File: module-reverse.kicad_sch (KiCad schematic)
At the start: 13 parts, among them J1 Screw_Terminal_01x02, J10 Screw_Terminal_01x05, J11 Screw_Terminal_01x05, J2 Screw_Terminal_01x02, J7 Screw_Terminal_01x02, J8 Screw_Terminal_01x02, J9 Screw_Terminal_01x02, K1 AZ733-2CE-12DE, U1 L7812

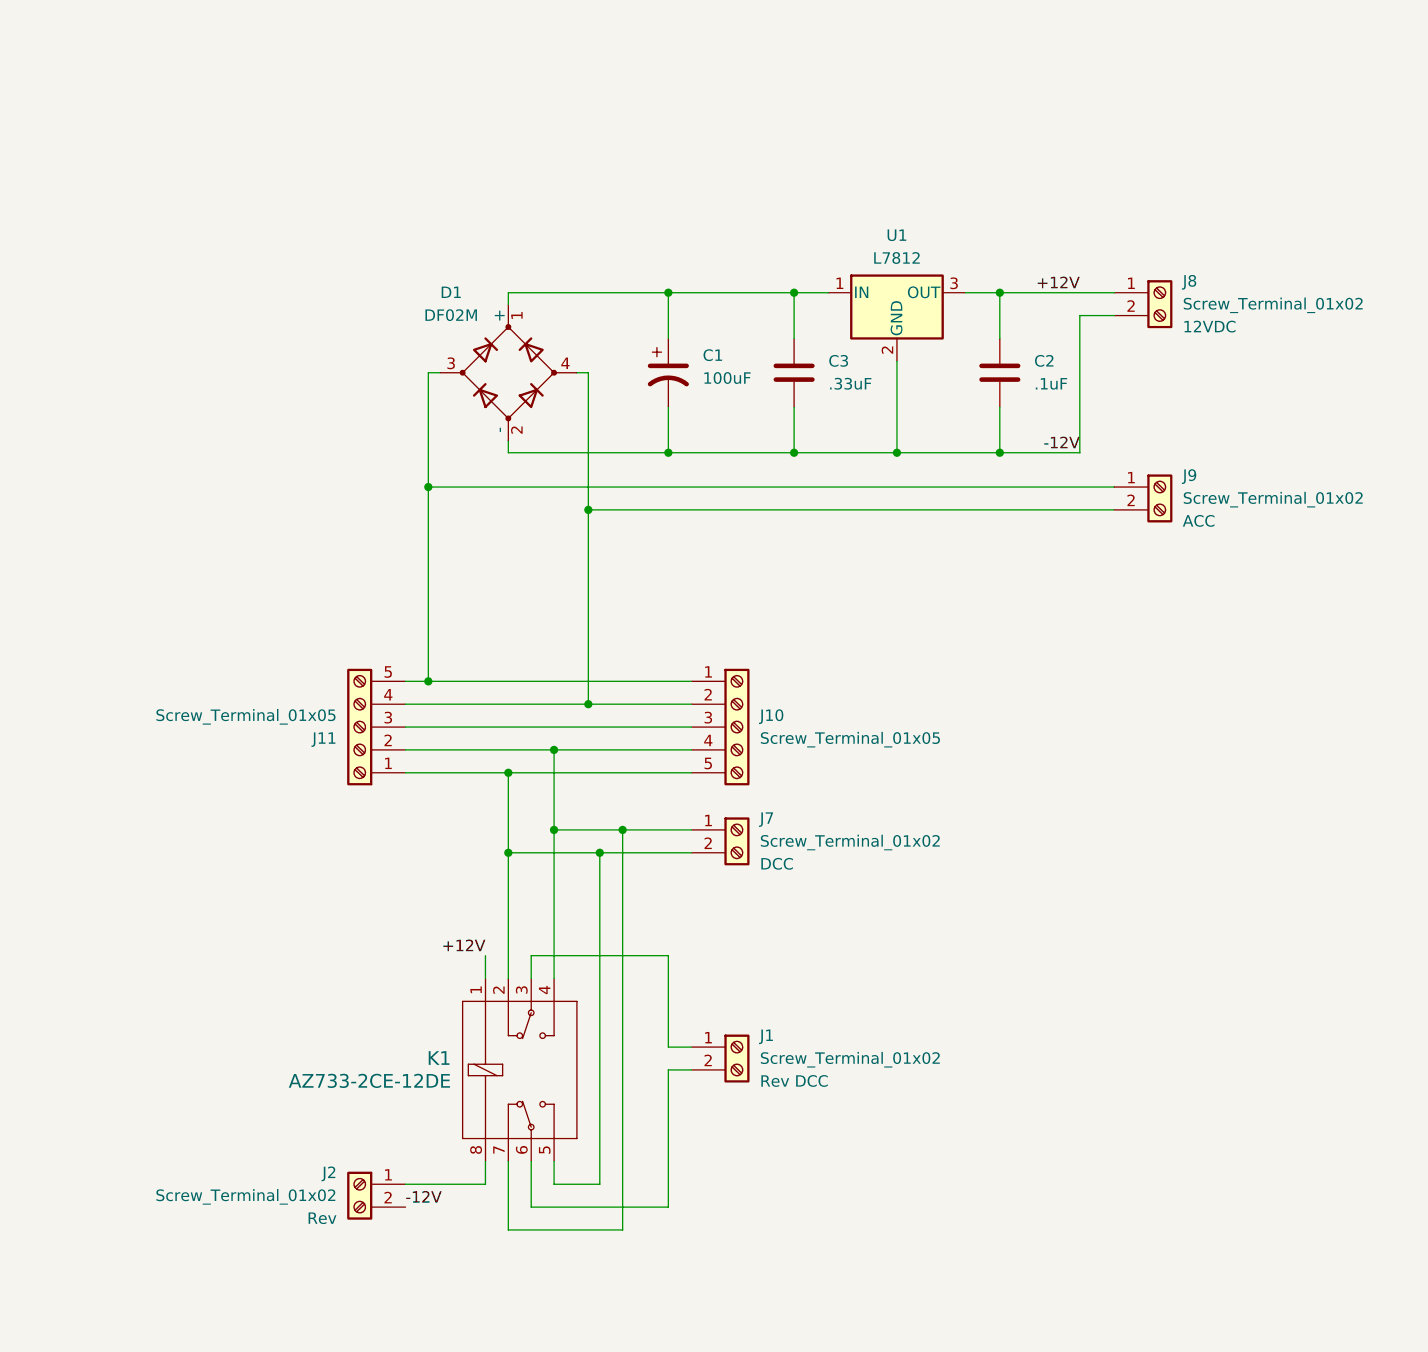
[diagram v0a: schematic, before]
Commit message: Changed the reversing output to have both Normal and Reverse outputs that go to the two branches instead of a single output that reverses.
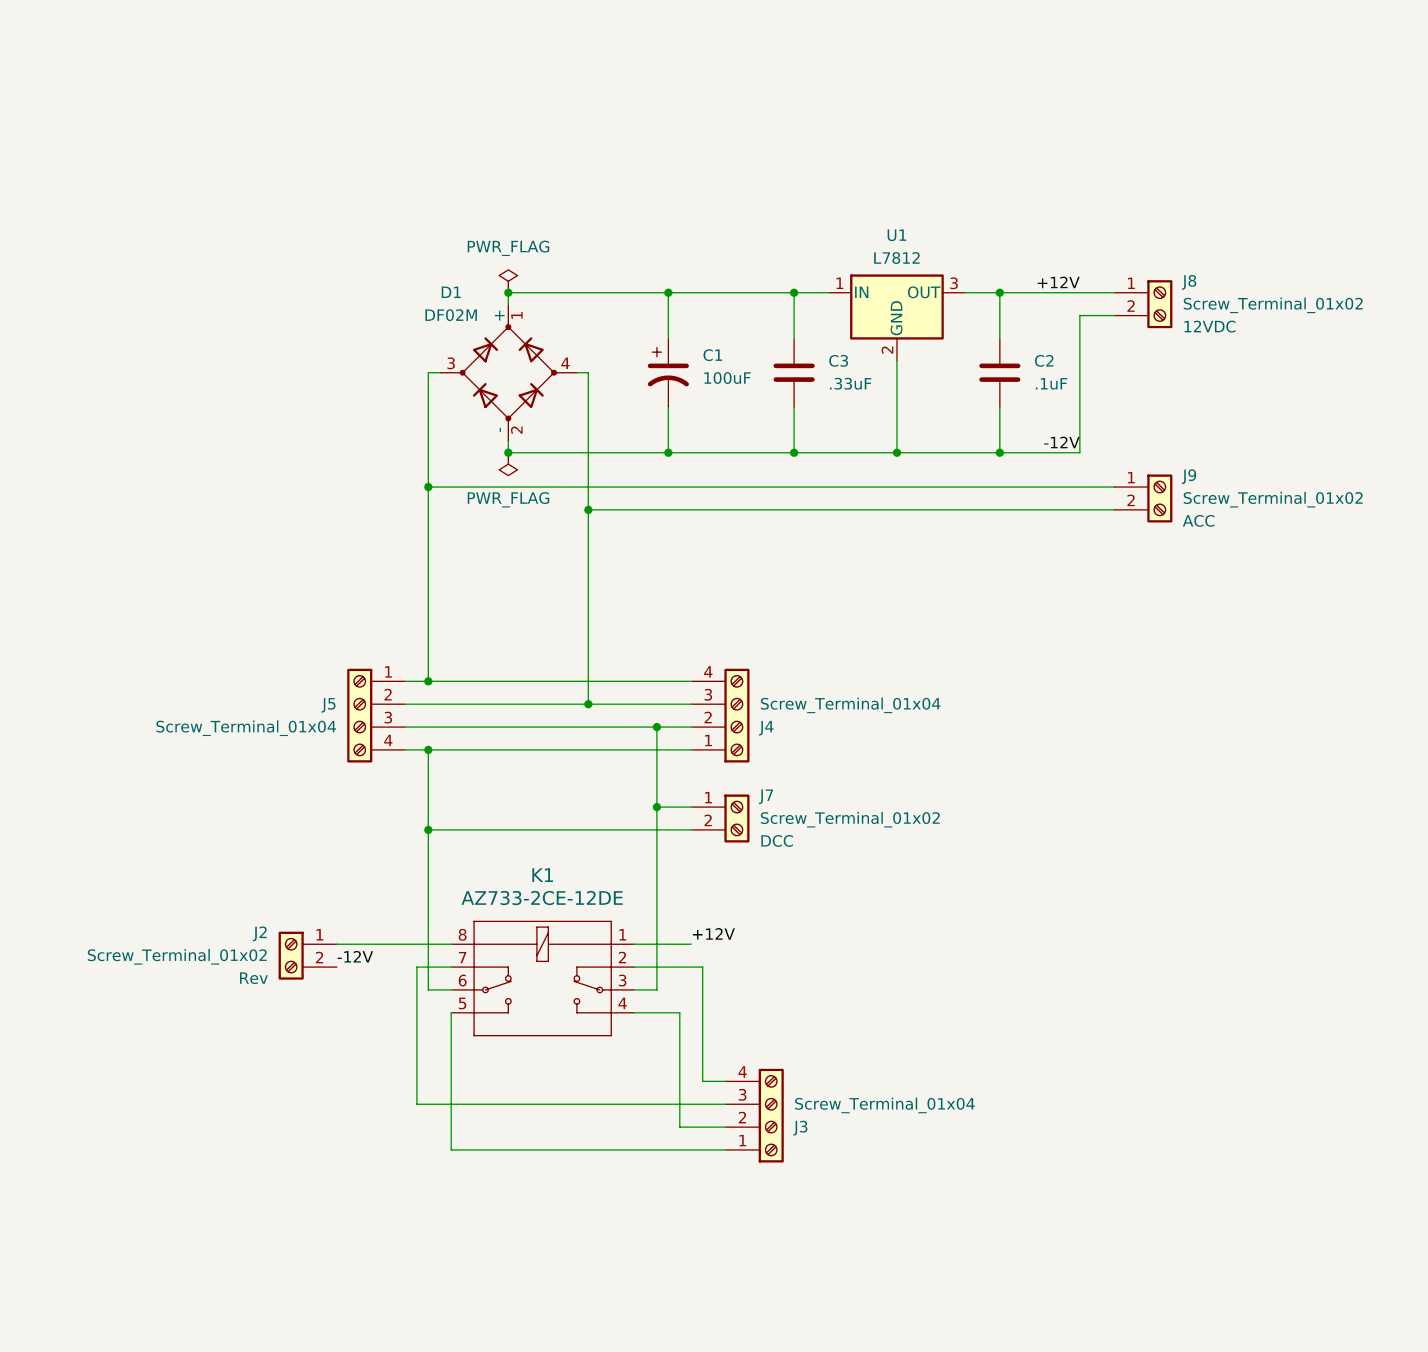
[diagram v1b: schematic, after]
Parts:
- removed J1: Screw_Terminal_01x02, Imports:CUI_TB005-762-02BE, symbol Connector:Screw_Terminal_01x02
- removed J10, J11: Screw_Terminal_01x05, Imports:CUI_TB005-762-05BE, symbol Connector:Screw_Terminal_01x05
- added J3, J4, J5: Screw_Terminal_01x04, Imports:CUI_TB005-762-04BE, symbol Connector:Screw_Terminal_01x04
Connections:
- net at D1.3, J9.1 (Pin_1): now also J4.4 (Pin_4), J5.1 (Pin_1)
- net at D1.4, J9.2 (Pin_2): now also J4.3 (Pin_3), J5.2 (Pin_2)
- net at K1.3: now also J7.1 (Pin_1), J4.2 (Pin_2), J5.3 (Pin_3)
- net at K1.6: now also J7.2 (Pin_2), J4.1 (Pin_1), J5.4 (Pin_4)
- new net: J3.1 (Pin_1), K1.5
- new net: J3.2 (Pin_2), K1.4
- new net: J3.3 (Pin_3), K1.7
- new net: J3.4 (Pin_4), K1.2
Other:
- moved on the sheet: J2, J7, K1

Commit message: Added LEDs
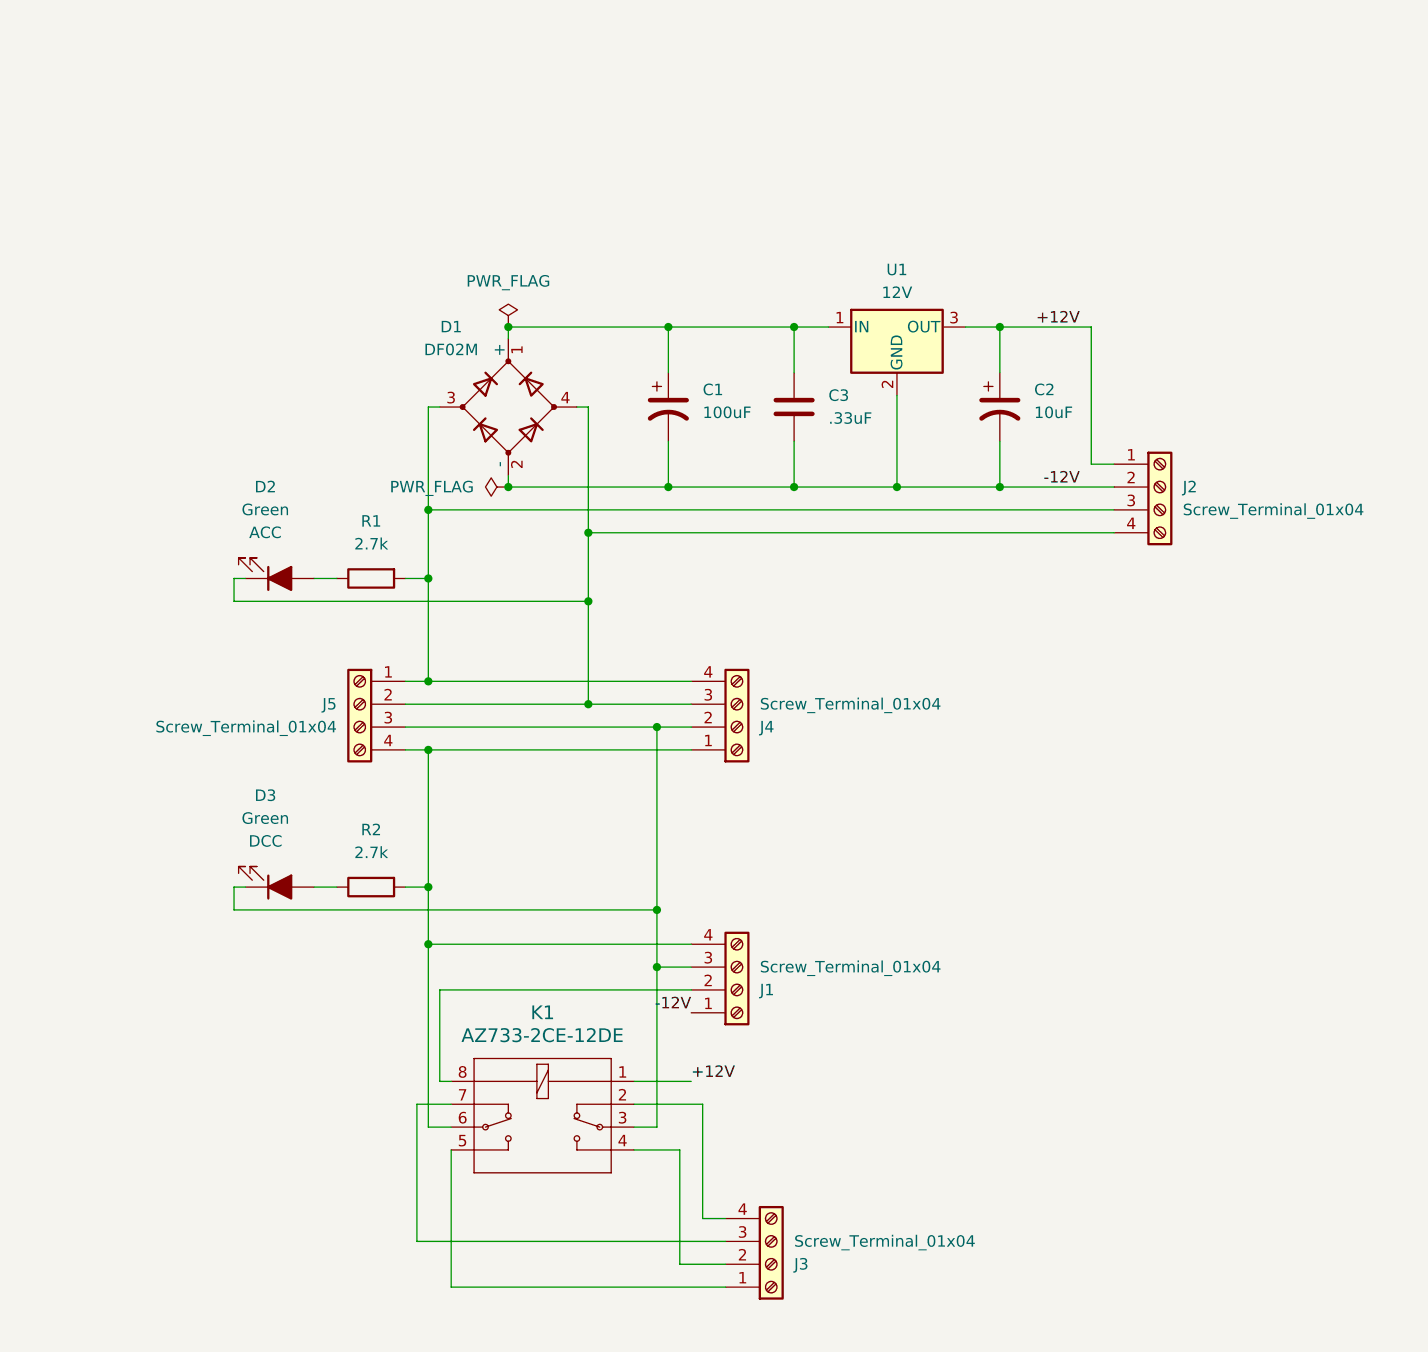
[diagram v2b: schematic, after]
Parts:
- removed J2, J7, J8, J9: Screw_Terminal_01x02, Imports:CUI_TB004-508-02BE, symbol Connector:Screw_Terminal_01x02
- added D2, D3: Green, LED_THT:LED_D3.0mm, symbol Device:LED_Filled
- added J1, J2: Screw_Terminal_01x04, Imports:CUI_TB005-762-04BE, symbol Connector:Screw_Terminal_01x04
- added R1, R2: 2.7k, Resistor_THT:R_Axial_DIN0207_L6.3mm_D2.5mm_P10.16mm_Horizontal, symbol Device:R
- C2: value .1uF -> 10uF; footprint Capacitor_THT:C_Disc_D5.0mm_W2.5mm_P5.00mm -> Capacitor_THT:CP_Radial_Tantal_D5.5mm_P5.00mm; symbol Device:C -> Device:C_Polarized_US; MPN FA28X7R1H104KNU00 -> TAP106K025CRS
- J3, J4, J5: MPN (none) -> TB005-762-04BE
- U1: value L7812 -> 12V; MPN L7812CV -> MIC2940A-12WT
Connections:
- net +12V: now also J2.1 (Pin_1)
- net -12V: now also J1.1 (Pin_1), J2.2 (Pin_2)
- net at D1.3, J4.4 (Pin_4), J5.1 (Pin_1): now also J2.3 (Pin_3), R1.2
- net at D1.4, J4.3 (Pin_3), J5.2 (Pin_2): now also D2.1 (K), J2.4 (Pin_4)
- net at K1.8: now also J1.2 (Pin_2)
- net at J4.2 (Pin_2), J5.3 (Pin_3), K1.3: now also D3.1 (K), J1.3 (Pin_3)
- net at J4.1 (Pin_1), J5.4 (Pin_4), K1.6: now also J1.4 (Pin_4), R2.2
- new net: D2.2 (A), R1.1
- new net: D3.2 (A), R2.1
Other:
- moved on the sheet: C1, C3, D1, J3, K1, U1

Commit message: Moved power to relay to before the voltage regulator
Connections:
- net +12V: now also C1.1, C3.1, D1.1 (+), U1.1 (IN); no longer C2.1, J2.1 (Pin_1), U1.3 (OUT)
- new net +Reg: C2.1, J2.1 (Pin_1), U1.3 (OUT)
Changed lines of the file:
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@@
     (stroke (width 0) (type default))
   )
-  (label "-12V" (at 179.07 77.47 180) (fields_autoplaced)
+  (label "-12V" (at 140.97 77.47 180) (fields_autoplaced)
     (effects (font (size 1.27 1.27)) (justify right bottom))
   )
@@
     (effects (font (size 1.27 1.27)) (justify right bottom))
   )
-  (label "+12V" (at 179.07 59.69 180) (fields_autoplaced)
+  (label "+12V" (at 142.24 59.69 180) (fields_autoplaced)
     (effects (font (size 1.27 1.27)) (justify right bottom))
   )
+  (label "+Reg" (at 173.99 59.69 0) (fields_autoplaced)
+    (effects (font (size 1.27 1.27)) (justify left bottom))
+  )
   (symbol (lib_id "Device:LED_Filled") (at 90.17 87.63 0) (mirror x) (unit 1)

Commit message: Updated to KiCad v8
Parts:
- U1: value 12V -> MIC2940A-12WT
